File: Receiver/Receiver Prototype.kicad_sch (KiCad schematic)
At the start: 35 parts, among them J1 Conn_01x02_Socket, J2 Conn_01x03, J4 Conn_Coaxial, J5 Conn_01x02, J6 Conn_01x02, J7 Conn_Coaxial, J8 Conn_Coaxial, U1 OPA3692ID, U2 AD8692ARZ

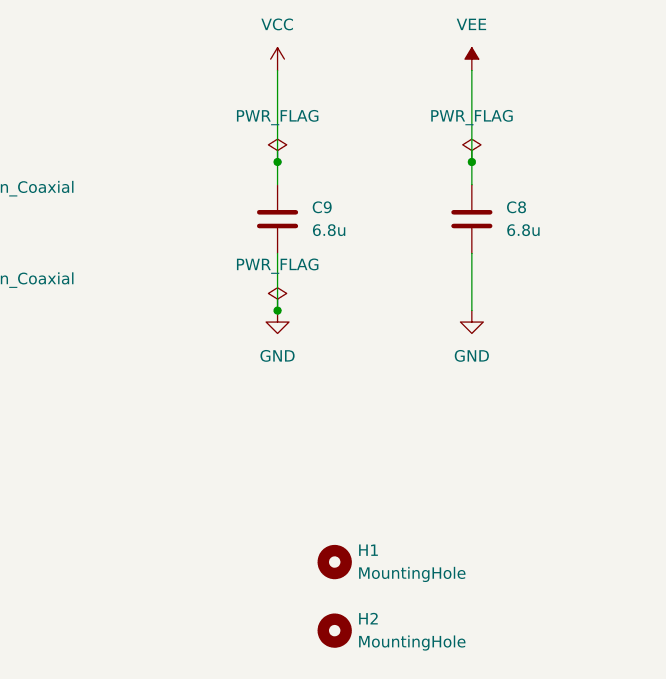
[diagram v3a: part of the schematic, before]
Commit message: Receiver PCB design v1 complete. DRC passed. Component's lables not added
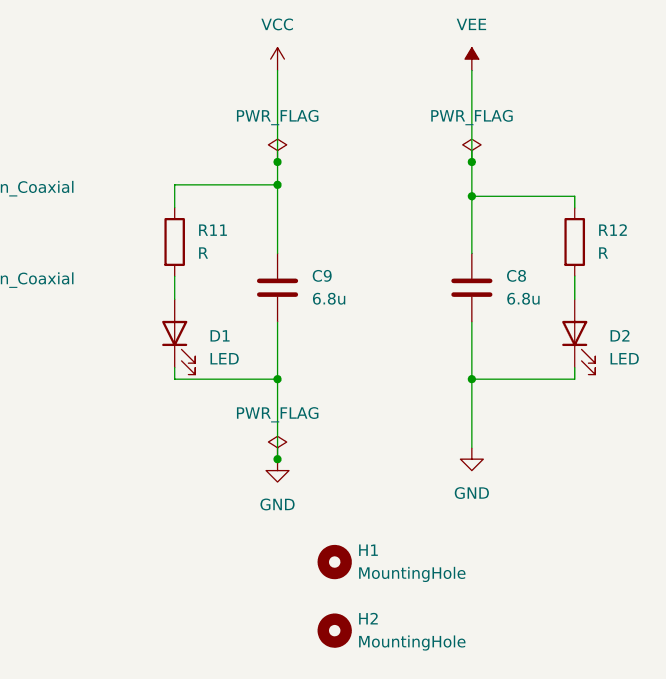
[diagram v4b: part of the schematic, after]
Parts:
- added D1, D2: LED, LED_SMD:LED_0805_2012Metric_Pad1.15x1.40mm_HandSolder, symbol Device:LED
- added R11, R12: R, Resistor_SMD:R_0805_2012Metric_Pad1.20x1.40mm_HandSolder, symbol Device:R
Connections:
- net GND: now also D1.1 (K), D2.1 (K)
- net VCC: now also R11.1
- net VEE: now also R12.1
- new net: D2.2 (A), R12.2
- new net: D1.2 (A), R11.2
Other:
- moved on the sheet: C8, C9

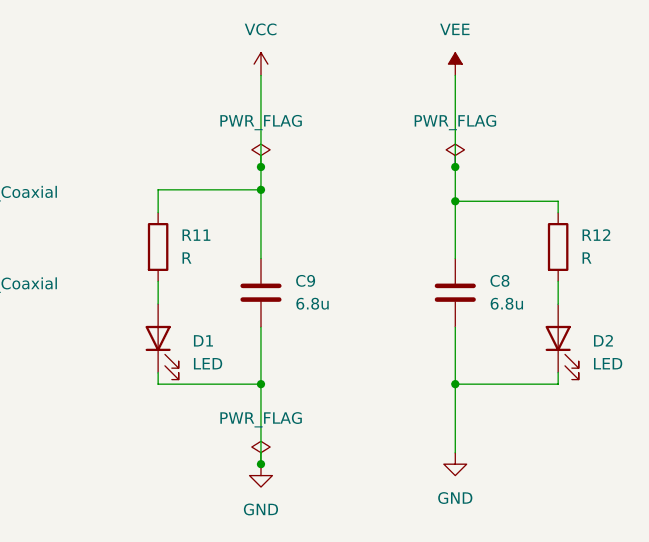
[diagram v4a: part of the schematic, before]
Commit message: This revision includes BNC connectors, SSOP packages, minor fixes and some basic lables
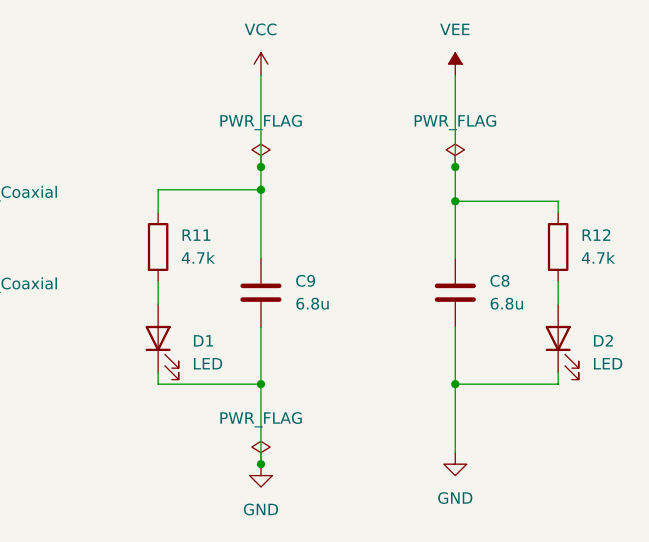
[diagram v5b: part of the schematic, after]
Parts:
- H1, H2, H3, H4: footprint MountingHole:MountingHole_2.5mm_Pad -> MountingHole:MountingHole_3.2mm_M3_Pad
- J4, J7, J8: footprint Connector_Coaxial:SMA_Amphenol_132134_Vertical -> BNC 112404:CONN_112404_AMP
- R11, R12: value R -> 4.7k
- U1: footprint OPA3692ID:D16 -> OPA3692 SSOP:DBQ16
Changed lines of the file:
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@@
 			)
 		)
-		(property "Value" "R"
+		(property "Value" "4.7k"
 			(at 304.8 55.8799 0)
 			(effects
@@
 			)
 		)
-		(property "Footprint" "OPA3692ID:D16"
+		(property "Footprint" "OPA3692 SSOP:DBQ16"
 			(at 74.93 76.2 0)
 			(effects
@@
 			)
 		)
-		(property "Footprint" "MountingHole:MountingHole_2.5mm_Pad"
+		(property "Footprint" "MountingHole:MountingHole_3.2mm_M3_Pad"
 			(at 275.59 90.17 0)
 			(effects
@@
 			)
 		)
-		(property "Footprint" "Connector_Coaxial:SMA_Amphenol_132134_Vertical"
+		(property "Footprint" "BNC 112404:CONN_112404_AMP"
 			(at 231.14 57.15 0)
 			(effects
@@
 			)
 		)
-		(property "Footprint" "Connector_Coaxial:SMA_Amphenol_132134_Vertical"
+		(property "Footprint" "BNC 112404:CONN_112404_AMP"
 			(at 73.66 52.07 0)
 			(effects
@@
 			)
 		)
-		(property "Value" "R"
+		(property "Value" "4.7k"
 			(at 260.35 55.8799 0)
 			(effects
@@
 			)
 		)
-		(property "Footprint" "MountingHole:MountingHole_2.5mm_Pad"
+		(property "Footprint" "MountingHole:MountingHole_3.2mm_M3_Pad"
 			(at 275.59 105.41 0)
 			(effects
@@
 			)
 		)
-		(property "Footprint" "MountingHole:MountingHole_2.5mm_Pad"
+		(property "Footprint" "MountingHole:MountingHole_3.2mm_M3_Pad"
 			(at 275.59 97.79 0)
 			(effects
@@
 			)
 		)
-		(property "Footprint" "Connector_Coaxial:SMA_Amphenol_132134_Vertical"
+		(property "Footprint" "BNC 112404:CONN_112404_AMP"
 			(at 231.14 46.99 0)
 			(effects
@@
 			)
 		)
-		(property "Footprint" "MountingHole:MountingHole_2.5mm_Pad"
+		(property "Footprint" "MountingHole:MountingHole_3.2mm_M3_Pad"
 			(at 275.59 113.03 0)
 			(effects

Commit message: minor fixes
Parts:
- R1: value 200 -> 200
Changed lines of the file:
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@@
 			)
 		)
-		(property "Value" "200"
+		(property "Value" "200 "
 			(at 54.61 90.17 90)
 			(effects

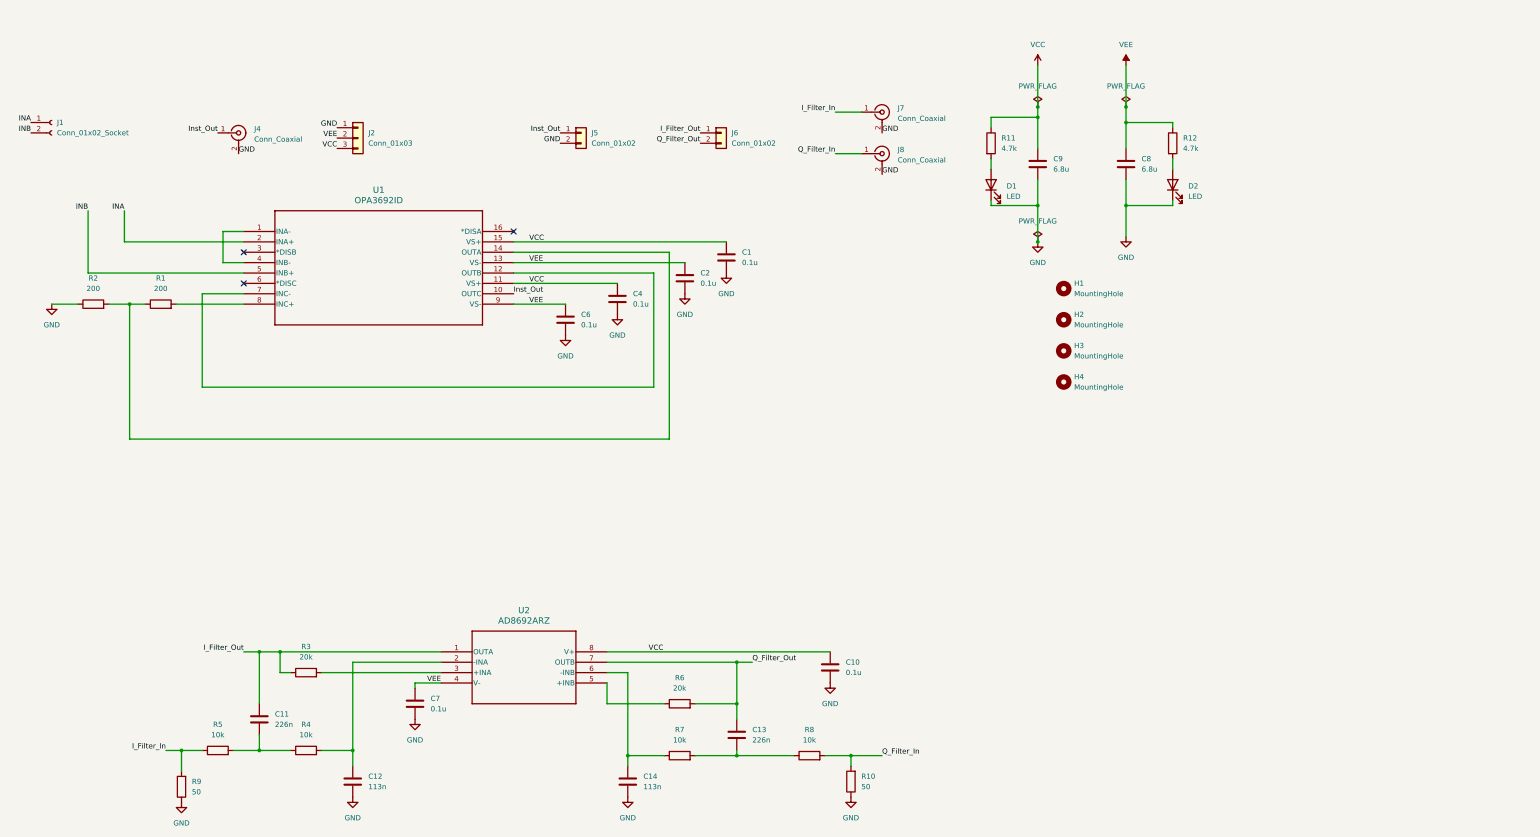
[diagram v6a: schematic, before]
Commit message: Added models for power regulators and OPA692 buffer. Also added diode clipper schematics
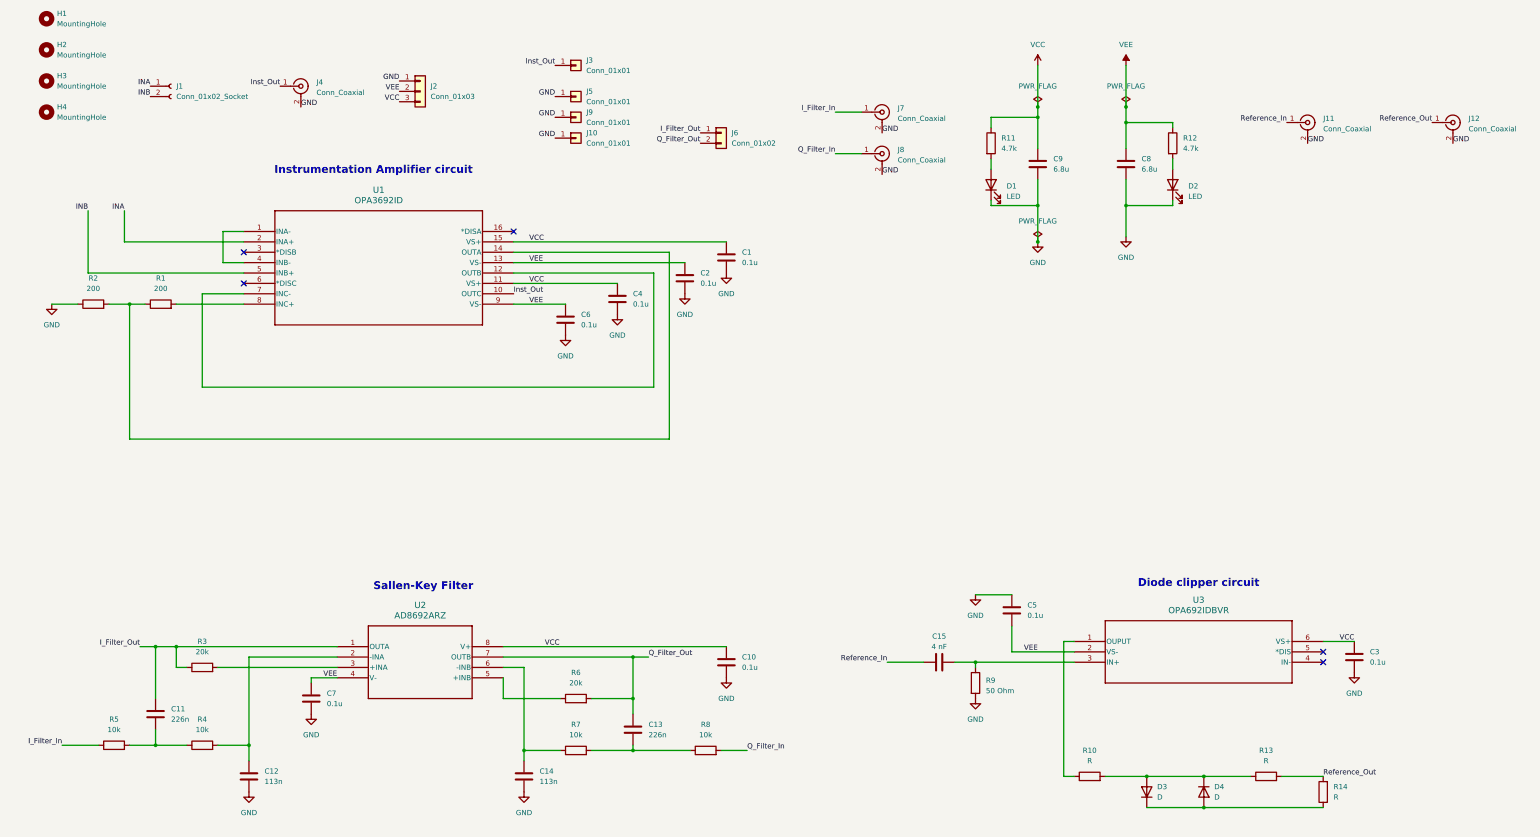
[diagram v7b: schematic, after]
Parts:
- removed J5: Conn_01x02, Connector_PinHeader_2.54mm:PinHeader_1x02_P2.54mm_Vertical, symbol Connector_Generic:Conn_01x02
- added C15: 4 nF, Capacitor_SMD:C_0805_2012Metric_Pad1.18x1.45mm_HandSolder, symbol Device:C
- added C3, C5: 0.1u, symbol Device:C
- added D3, D4: D, symbol Device:D
- added J10, J3, J5, J9: Conn_01x01, symbol Connector_Generic:Conn_01x01
- added J11, J12: Conn_Coaxial, BNC 112404:CONN_112404_AMP, symbol Connector:Conn_Coaxial
- added R13, R14: R, symbol Device:R
- added U3: OPA692IDBVR, DBV6, symbol OPA692 SOT-23:OPA692IDBVR
- R10: value 50 -> R; footprint Resistor_SMD:R_0805_2012Metric_Pad1.20x1.40mm_HandSolder -> (none)
- R9: value 50 -> 50 Ohm
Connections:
- net GND: now also R9.2, C3.2, C5.1, J10.1 (Pin_1), J11.2 (Ext), J12.2 (Ext), J5.1 (Pin_1), J9.1 (Pin_1); no longer R10.1, R9.1
- net I_Filter_In: no longer R9.2
- net Inst_Out: now also J3.1 (Pin_1)
- net Q_Filter_In: no longer R10.2
- net VCC: now also C3.1, U3.6 (VS+)
- net VEE: now also C5.2, U3.2 (VS-)
- new net: D3.2 (A), D4.1 (K), R10.2, R13.1
- new net: R10.1, U3.1 (OUPUT)
- new net: D3.1 (K), D4.2 (A), R14.1
- new net: C15.2, R9.1, U3.3 (IN+)
- new net Reference_In: C15.1, J11.1 (In)
- new net Reference_Out: J12.1 (In), R13.2, R14.2
- no-connect marks 3 -> 5
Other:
- note added: "Diode clipper circuit"
- note added: "Instrumentation Amplifier circuit"
- note added: "Sallen-Key Filter"
- moved on the sheet: C10, C11, C12, C13, C14, C7, H1, H2, H3, H4, J1, J2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

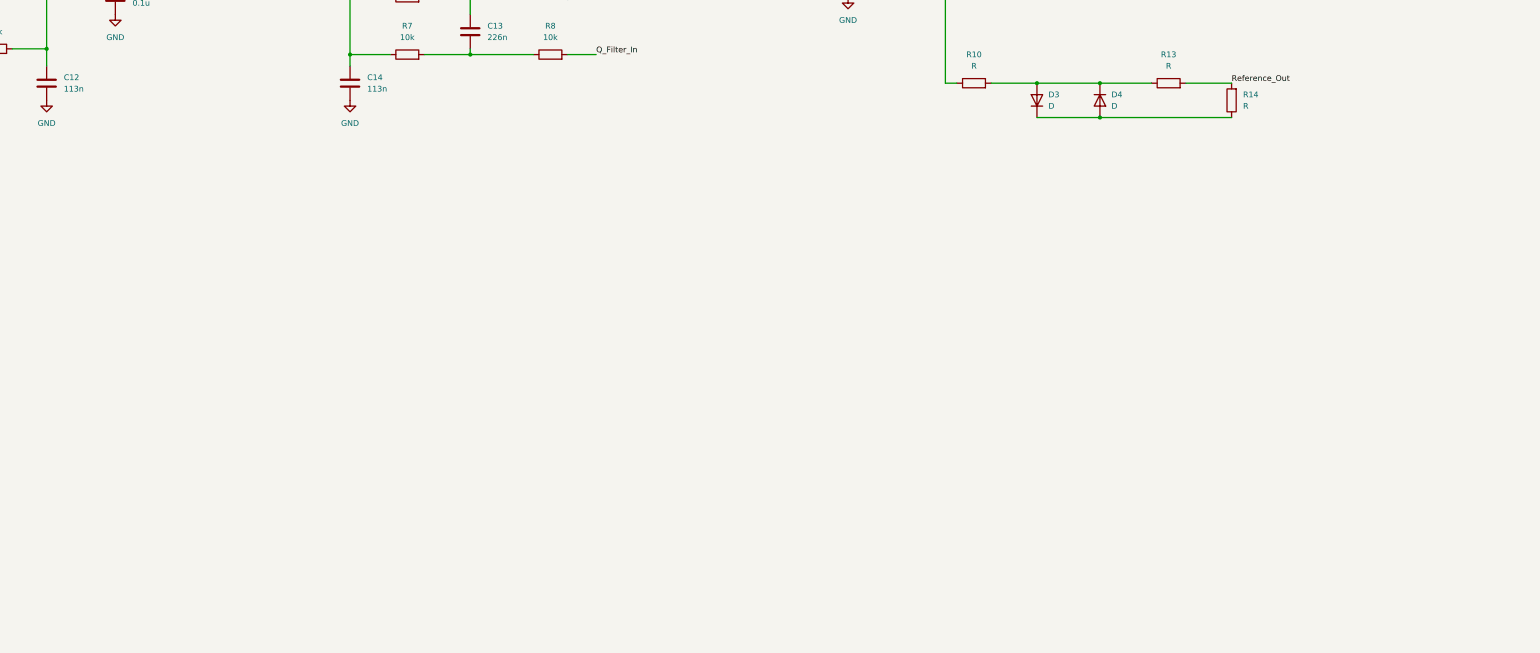
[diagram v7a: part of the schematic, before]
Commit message: Added AD607 to schematic
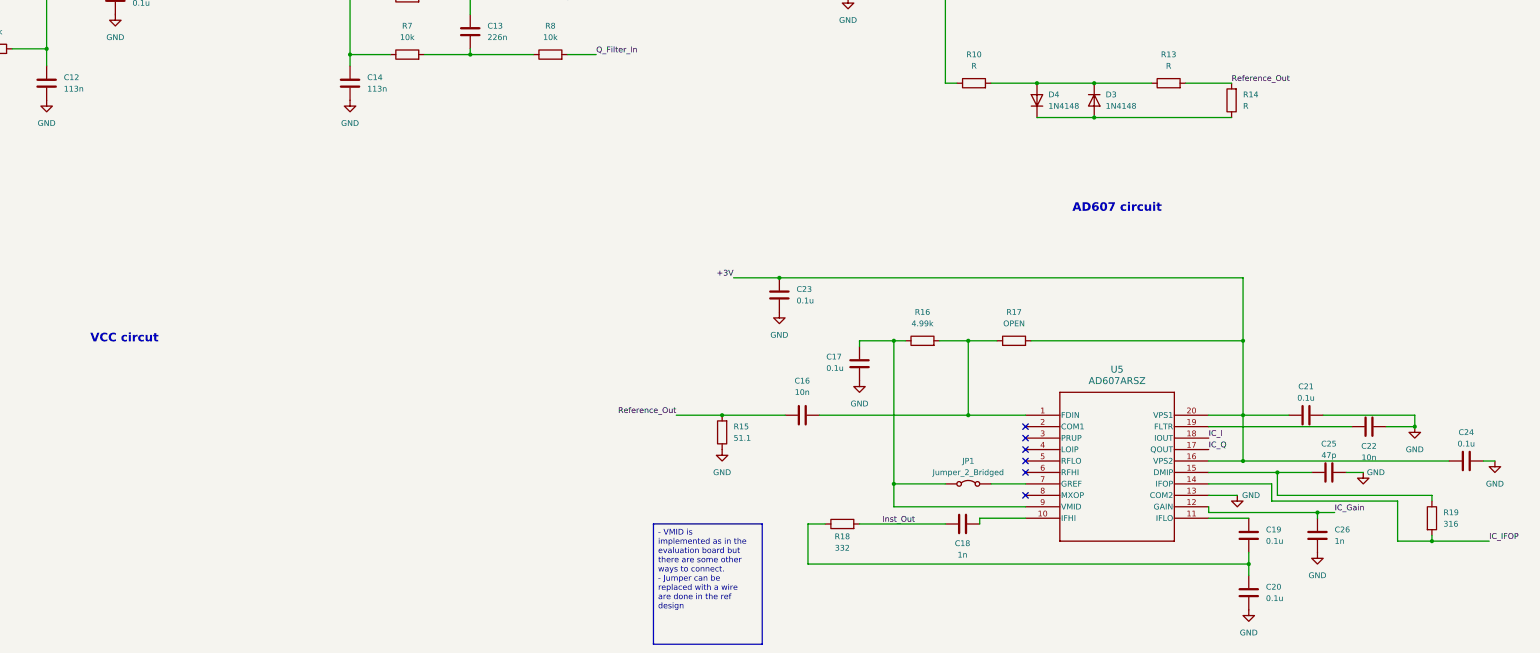
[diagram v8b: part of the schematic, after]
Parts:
- removed D3, D4: D, symbol Device:D
- added C16, C22: 10n, Capacitor_SMD:C_0603_1608Metric_Pad1.08x0.95mm_HandSolder, symbol Device:C
- added C17, C19, C20, C21, C23, C24: 0.1u, Capacitor_SMD:C_0603_1608Metric_Pad1.08x0.95mm_HandSolder, symbol Device:C
- added C18, C26: 1n, Capacitor_SMD:C_0603_1608Metric_Pad1.08x0.95mm_HandSolder, symbol Device:C
- added C25: 47p, Capacitor_SMD:C_0603_1608Metric_Pad1.08x0.95mm_HandSolder, symbol Device:C
- added D3, D4: 1N4148, Diode_THT:D_DO-35_SOD27_P7.62mm_Horizontal, symbol Diode:1N4148
- added JP1: Jumper_2_Bridged, symbol Jumper:Jumper_2_Bridged
- added R15: 51.1, Resistor_SMD:R_0603_1608Metric_Pad0.98x0.95mm_HandSolder, symbol Device:R
- added R16: 4.99k, Resistor_SMD:R_0603_1608Metric_Pad0.98x0.95mm_HandSolder, symbol Device:R
- added R17: OPEN, Resistor_SMD:R_0603_1608Metric_Pad0.98x0.95mm_HandSolder, symbol Device:R
- added R18: 332, Resistor_SMD:R_0603_1608Metric_Pad0.98x0.95mm_HandSolder, symbol Device:R
- added R19: 316, Resistor_SMD:R_0603_1608Metric_Pad0.98x0.95mm_HandSolder, symbol Device:R
- added U5: AD607ARSZ, AD607ARSZ:RS_20_ADI, symbol AD607ARSZ:AD607ARSZ
- C1, C10, C11, C12, C13, C14, C15, C2, C4, C6, C7, C8, C9: footprint Capacitor_SMD:C_0805_2012Metric_Pad1.18x1.45mm_HandSolder -> Capacitor_SMD:C_0603_1608Metric_Pad1.08x0.95mm_HandSolder
- C3, C5: footprint (none) -> Capacitor_SMD:C_0603_1608Metric_Pad1.08x0.95mm_HandSolder
- D1, D2: footprint LED_SMD:LED_0805_2012Metric_Pad1.15x1.40mm_HandSolder -> LED_SMD:LED_0603_1608Metric_Pad1.05x0.95mm_HandSolder
- J10, J3, J5, J9: footprint (none) -> Connector_PinSocket_2.54mm:PinSocket_1x01_P2.54mm_Vertical
- R1, R11, R12, R2, R3, R4, R5, R6, R7, R8, R9: footprint Resistor_SMD:R_0805_2012Metric_Pad1.20x1.40mm_HandSolder -> Resistor_SMD:R_0603_1608Metric_Pad0.98x0.95mm_HandSolder
- R10, R13, R14: footprint (none) -> Resistor_SMD:R_0603_1608Metric_Pad0.98x0.95mm_HandSolder
- U3: footprint DBV6 -> OPA692 SOT-23:DBV6
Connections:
- net GND: now also C17.1, C20.2, C21.2, C22.2, C23.1, C24.2, C25.2, C26.2, R15.1, U5.13 (COM2)
- net Inst_Out: now also C18.1, R18.2
- net Reference_Out: now also C16.1, R15.2
- net at R10.2, R13.1: now also D3.1 (K), D4.2 (A)
- net at R14.1: now also D3.2 (A), D4.1 (K)
- new net: C25.1, R19.1, U5.15 (DMIP)
- new net: C19.2, C20.1, R18.1
- new net: C16.2, R16.2, R17.1, U5.1 (FDIN)
- new net: C18.2, U5.10 (IFHI)
- new net: C19.1, U5.11 (IFLO)
- new net: C22.1, U5.19 (FLTR)
- new net: JP1.2 (B), U5.7 (GREF)
- new net: C17.2, JP1.1 (A), R16.1, U5.9 (VMID)
- new net +3V: C21.1, C23.2, C24.1, R17.2, U5.16 (VPS2), U5.20 (VPS1)
- new net IC_Gain: C26.1, U5.12 (GAIN)
- new net IC_I: U5.18 (IOUT)
- new net IC_IFOP: R19.2, U5.14 (IFOP)
- new net IC_Q: U5.17 (QOUT)
- no-connect marks 5 -> 11
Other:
- note added: "AD607 circuit"
- note added: "VCC circut"
